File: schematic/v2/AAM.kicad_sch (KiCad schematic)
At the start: 1 part, among them U17 NUCLEO-H753ZI

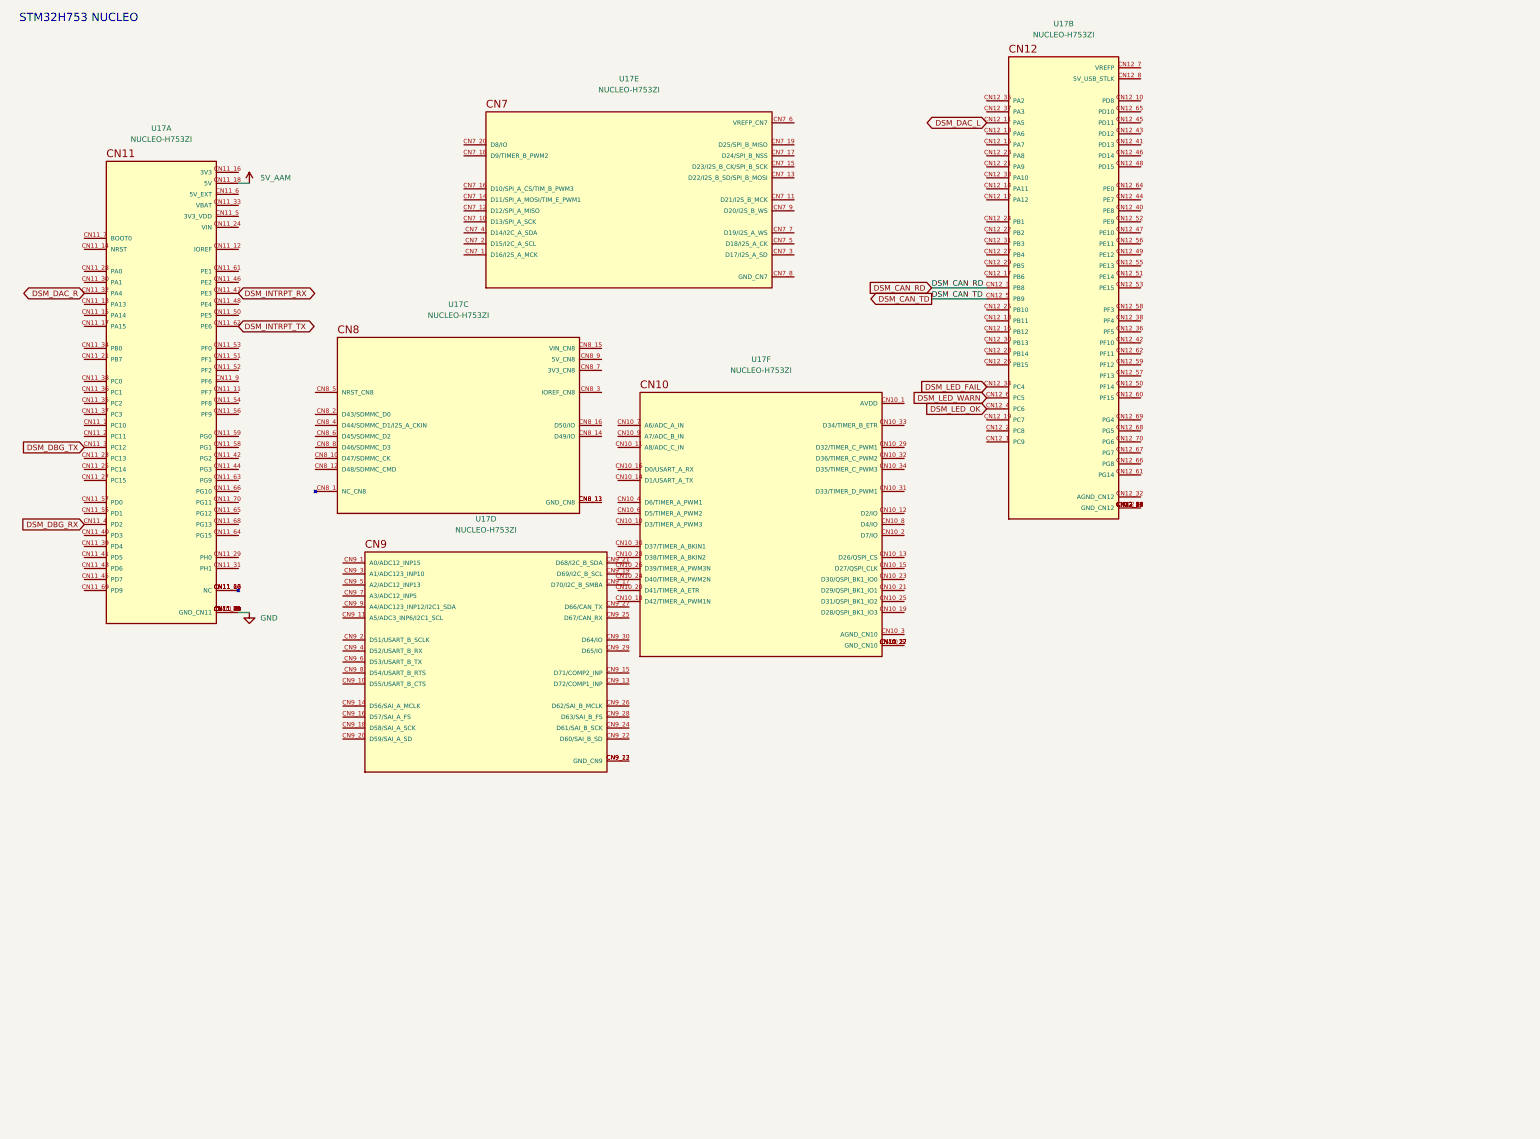
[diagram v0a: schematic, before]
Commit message: moving to multiple sheets for the schematic
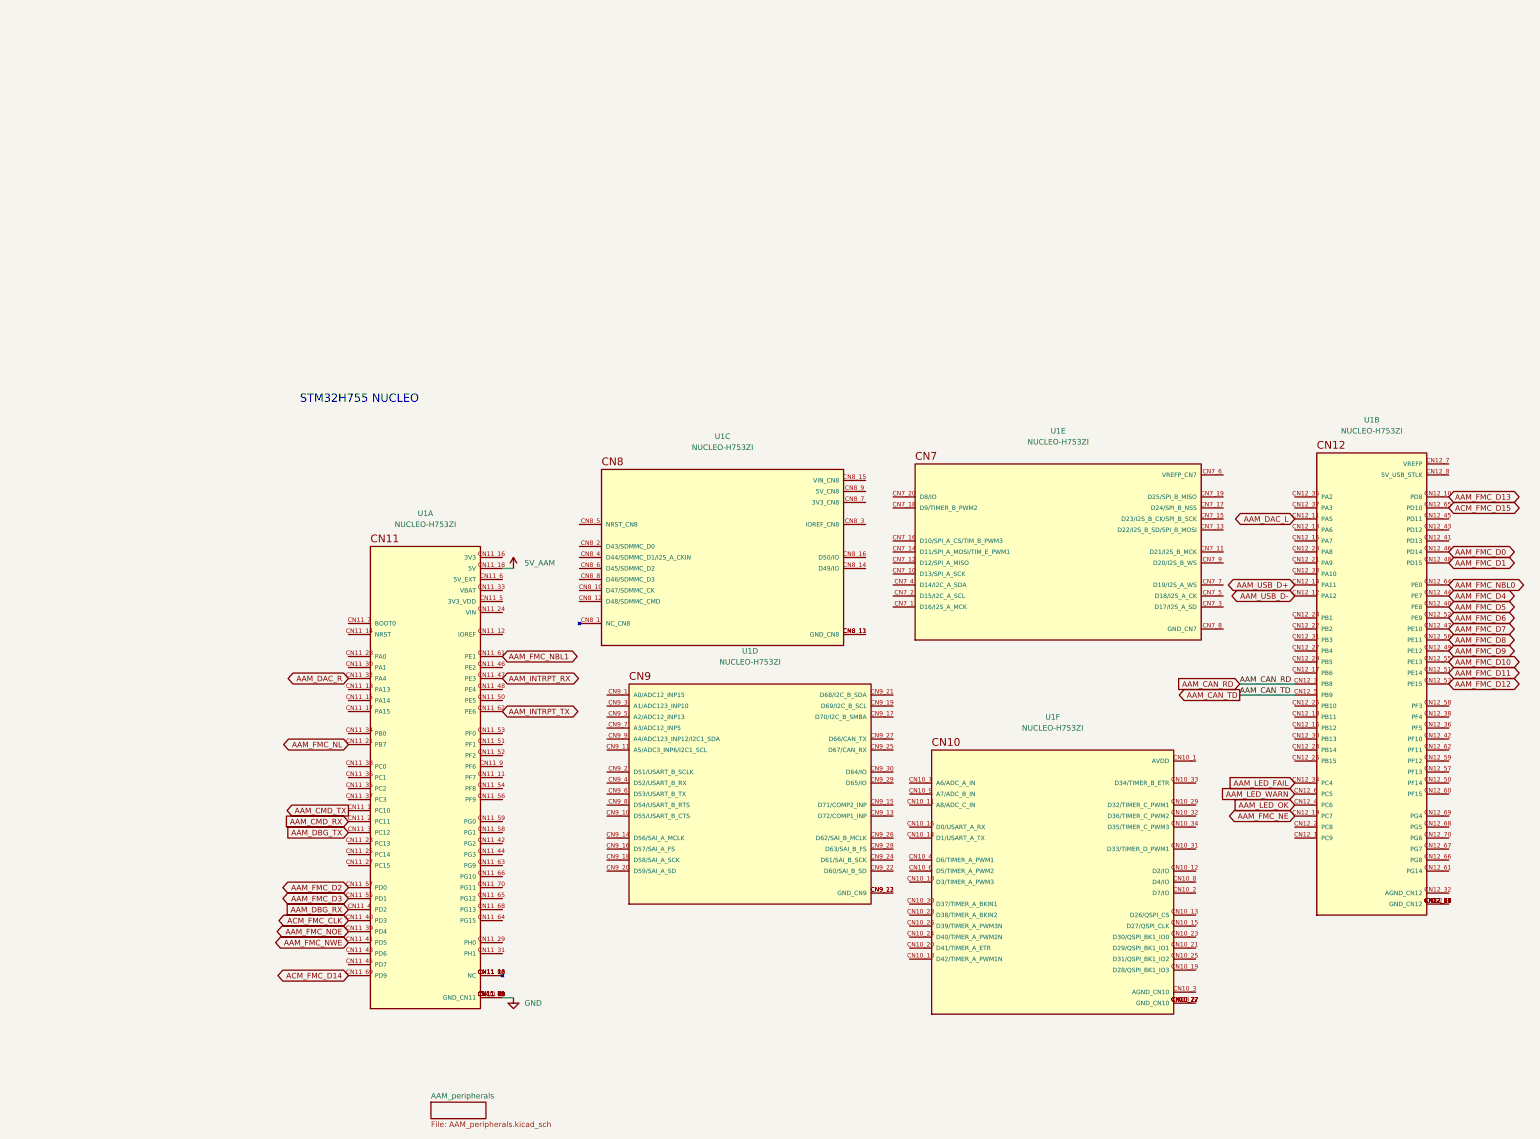
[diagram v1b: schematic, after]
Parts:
- removed U17: NUCLEO-H753ZI, NUCLEO-H753ZI:MODULE_NUCLEO-H753ZI, symbol NUCLEO-H753ZI:NUCLEO-H753ZI
- added U1: NUCLEO-H753ZI, NUCLEO-H753ZI:MODULE_NUCLEO-H753ZI, symbol NUCLEO-H753ZI:NUCLEO-H753ZI
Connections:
- net 5V_AAM: now also U1.CN11_18 (5V)
- net GND: now also U1.CN11_19 (GND_CN11), U1.CN11_20 (GND_CN11), U1.CN11_22 (GND_CN11), U1.CN11_49 (GND_CN11), U1.CN11_60 (GND_CN11), U1.CN11_71 (GND_CN11), U1.CN11_72 (GND_CN11), U1.CN11_8 (GND_CN11)
- new net: U1.CN9_12 (GND_CN9), U1.CN9_23 (GND_CN9)
- new net: U1.CN11_10 (NC), U1.CN11_26 (NC), U1.CN11_67 (NC)
- new net: U1.CN10_17 (GND_CN10), U1.CN10_22 (GND_CN10), U1.CN10_27 (GND_CN10), U1.CN10_5 (GND_CN10)
- new net: U1.CN12_20 (GND_CN12), U1.CN12_39 (GND_CN12), U1.CN12_54 (GND_CN12), U1.CN12_63 (GND_CN12), U1.CN12_71 (GND_CN12), U1.CN12_72 (GND_CN12), U1.CN12_9 (GND_CN12)
- new net: U1.CN8_11 (GND_CN8), U1.CN8_13 (GND_CN8)
- new net AAM_CAN_RD: U1.CN12_3 (PB8)
- new net AAM_CAN_TD: U1.CN12_5 (PB9)
- new net AAM_CMD_RX: U1.CN11_2 (PC11)
- new net AAM_CMD_TX: U1.CN11_1 (PC10)
- new net AAM_DAC_L: U1.CN12_11 (PA5)
- new net AAM_DAC_R: U1.CN11_32 (PA4)
- new net AAM_DBG_RX: U1.CN11_4 (PD2)
- new net AAM_DBG_TX: U1.CN11_3 (PC12)
- new net AAM_FMC_D0: U1.CN12_46 (PD14)
- new net AAM_FMC_D1: U1.CN12_48 (PD15)
- new net AAM_FMC_D10: U1.CN12_55 (PE13)
- new net AAM_FMC_D11: U1.CN12_51 (PE14)
- new net AAM_FMC_D12: U1.CN12_53 (PE15)
- new net AAM_FMC_D13: U1.CN12_10 (PD8)
- new net AAM_FMC_D2: U1.CN11_57 (PD0)
- new net AAM_FMC_D3: U1.CN11_55 (PD1)
- new net AAM_FMC_D4: U1.CN12_44 (PE7)
- new net AAM_FMC_D5: U1.CN12_40 (PE8)
- new net AAM_FMC_D6: U1.CN12_52 (PE9)
- new net AAM_FMC_D7: U1.CN12_47 (PE10)
- new net AAM_FMC_D8: U1.CN12_56 (PE11)
- new net AAM_FMC_D9: U1.CN12_49 (PE12)
- new net AAM_FMC_NBL0: U1.CN12_64 (PE0)
- new net AAM_FMC_NBL1: U1.CN11_61 (PE1)
- new net AAM_FMC_NE: U1.CN12_19 (PC7)
- new net AAM_FMC_NL: U1.CN11_21 (PB7)
- new net AAM_FMC_NOE: U1.CN11_39 (PD4)
- new net AAM_FMC_NWE: U1.CN11_41 (PD5)
- new net AAM_INTRPT_RX: U1.CN11_47 (PE3)
- new net AAM_INTRPT_TX: U1.CN11_62 (PE6)
- new net AAM_LED_FAIL: U1.CN12_34 (PC4)
- new net AAM_LED_OK: U1.CN12_4 (PC6)
- new net AAM_LED_WARN: U1.CN12_6 (PC5)
- new net AAM_USB_D+: U1.CN12_14 (PA11)
- new net AAM_USB_D-: U1.CN12_12 (PA12)
- new net ACM_FMC_CLK: U1.CN11_40 (PD3)
- new net ACM_FMC_D14: U1.CN11_69 (PD9)
- new net ACM_FMC_D15: U1.CN12_65 (PD10)
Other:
- added sheet AAM_peripherals (AAM_peripherals.kicad_sch)
- note added: "STM32H755 NUCLEO"
- note removed: "STM32H753 NUCLEO"

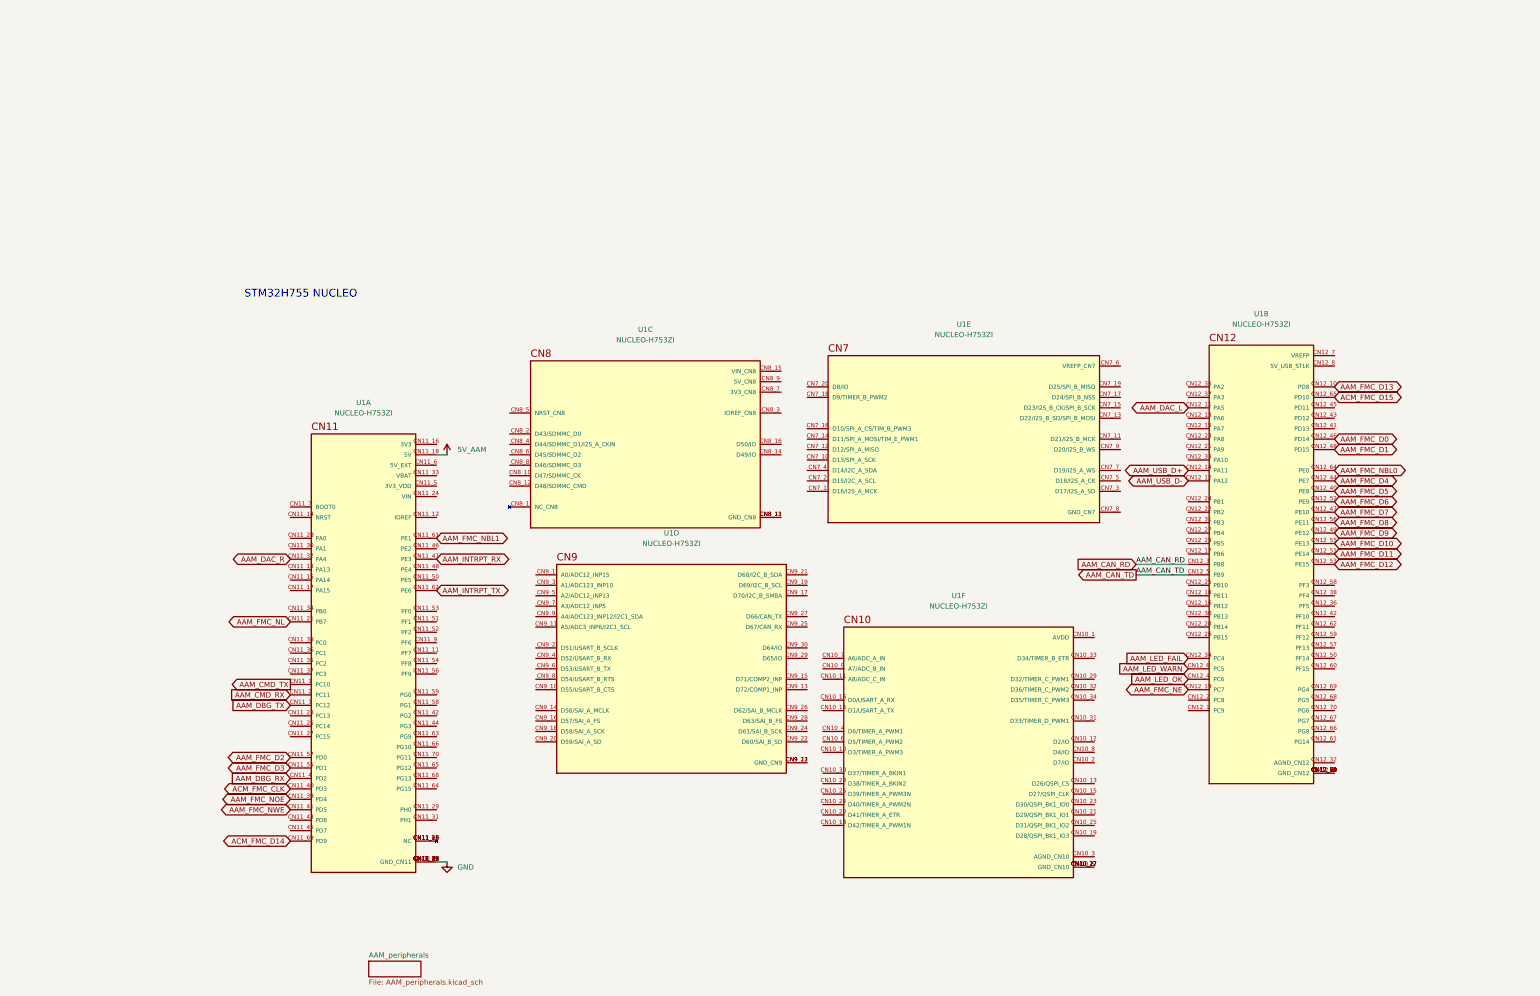
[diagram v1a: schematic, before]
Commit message: adding more sheets in the schematic
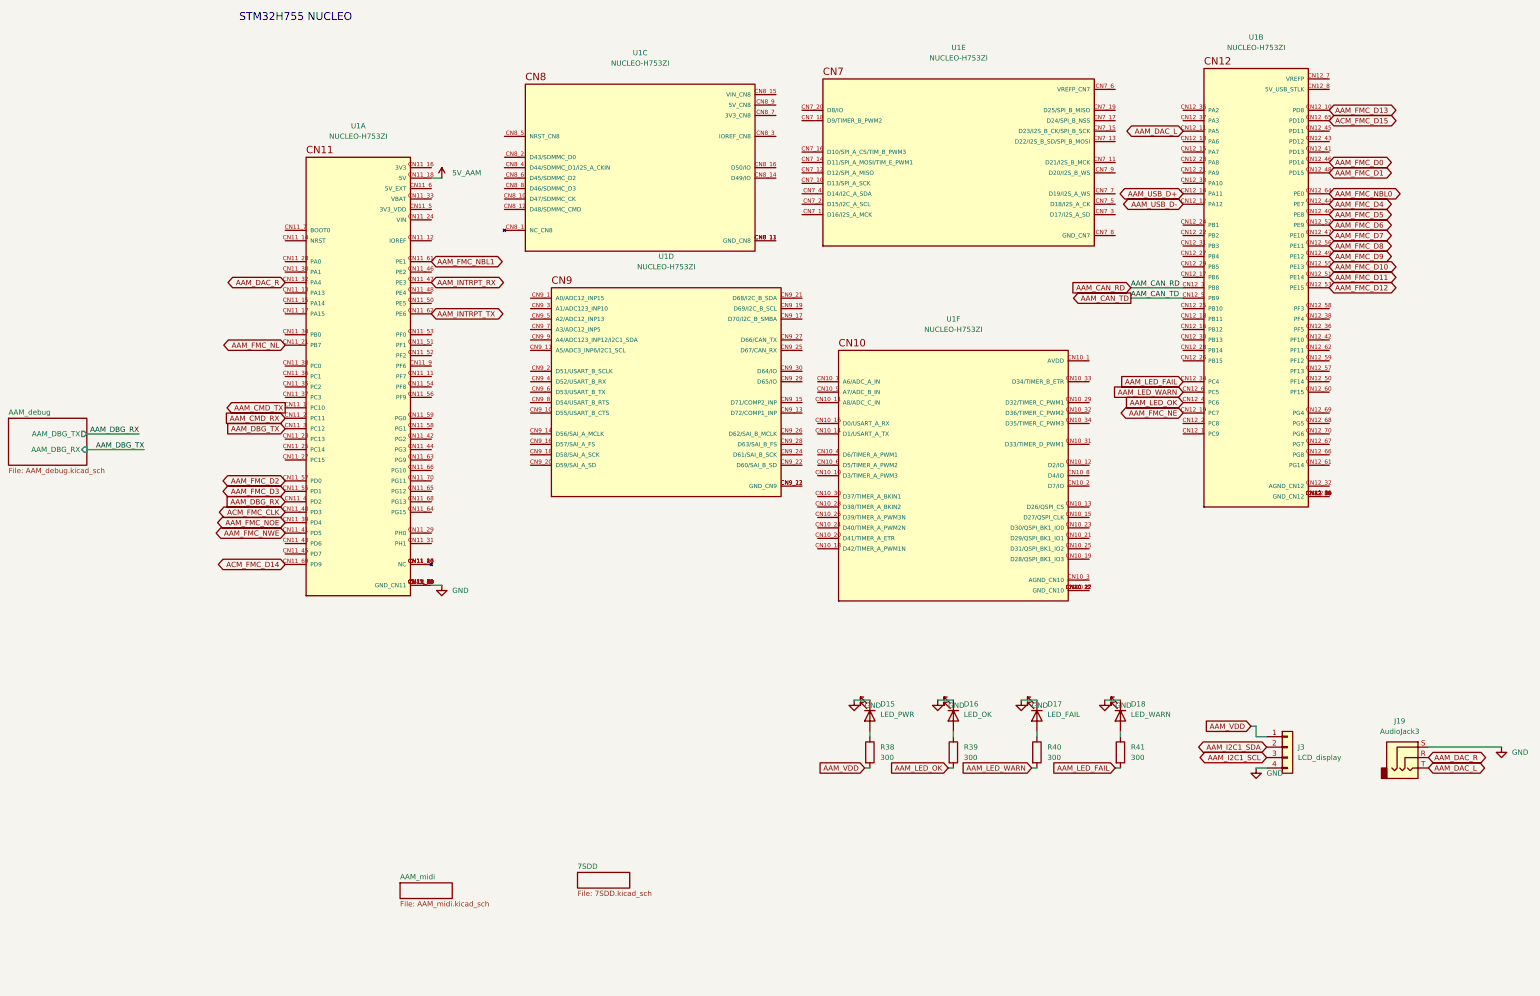
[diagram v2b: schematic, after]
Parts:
- added D15: LED_PWR, LED_SMD:LED_0603_1608Metric, symbol Device:LED
- added D16: LED_OK, LED_SMD:LED_0603_1608Metric, symbol Device:LED
- added D17: LED_FAIL, LED_SMD:LED_0603_1608Metric, symbol Device:LED
- added D18: LED_WARN, LED_SMD:LED_0603_1608Metric, symbol Device:LED
- added J19: AudioJack3, Connector_Audio:Jack_3.5mm_CUI_SJ-3523-SMT_Horizontal, symbol Connector_Audio:AudioJack3
- added J3: LCD_display, Connector_PinHeader_1.00mm:PinHeader_1x04_P1.00mm_Vertical_SMD_Pin1Left, symbol Connector_Generic:Conn_01x04
- added R38, R39, R40, R41: 300, Resistor_SMD:R_0805_2012Metric_Pad1.20x1.40mm_HandSolder, symbol Device:R
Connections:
- net AAM_DAC_L: now also J19.T
- net AAM_DAC_R: now also J19.R
- net AAM_LED_FAIL: now also R41.2
- net AAM_LED_OK: now also R39.2
- net AAM_LED_WARN: now also R40.2
- net GND: now also D15.1 (K), D16.1 (K), D17.1 (K), D18.1 (K), J19.S, J3.4 (Pin_4)
- new net: D18.2 (A), R41.1
- new net: D15.2 (A), R38.1
- new net: D16.2 (A), R39.1
- new net: D17.2 (A), R40.1
- new net AAM_I2C1_SCL: J3.3 (Pin_3)
- new net AAM_I2C1_SDA: J3.2 (Pin_2)
- new net AAM_VDD: J3.1 (Pin_1), R38.2
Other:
- removed sheet AAM_peripherals
- added sheet 7SDD (7SDD.kicad_sch)
- added sheet AAM_debug (AAM_debug.kicad_sch)
- added sheet AAM_midi (AAM_midi.kicad_sch)
- moved on the sheet: U1A, U1B, U1C, U1D, U1E, U1F

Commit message: progress on putting things in different sheets
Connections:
- net ACM_FMC_CLK renamed AAM_FMC_CLK
- net ACM_FMC_D14 renamed AAM_FMC_D14
- net ACM_FMC_D15 renamed AAM_FMC_D15
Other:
- sheet 7SDD ports: added 7SDD_CMD_RX, 7SDD_CMD_TX; removed none
- sheet AAM_midi ports: added AAM_USB_D+, AAM_USB_D-; removed none
- moved on the sheet: D15, D16, D17, D18, J19, J3, R38, R39, R40, R41, U1A, U1B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

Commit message: v2 updates. remove sniffer
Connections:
- net AAM_I2C1_SCL is gone; now on net APM_I2C1_SCL: J3.3 (Pin_3)
- net AAM_I2C1_SDA is gone; now on net APM_I2C1_SDA: J3.2 (Pin_2)
- net APM_I2C1_SCL: now reaches U1.CN11_51 (PF1)
- net APM_I2C1_SDA: now reaches U1.CN11_53 (PF0)
- net 5V_AAM renamed 5V_APM
- net AAM_CAN_RD renamed APM_CAN_RD
- net AAM_CAN_TD renamed APM_CAN_TD
- net AAM_CMD_RX renamed APM_CMD_RX
- net AAM_CMD_TX renamed APM_CMD_TX
- net AAM_DAC_L renamed APM_DAC_L
- net AAM_DAC_R renamed APM_DAC_R
- net AAM_DBG_RX renamed APM_DBG_RX
- net AAM_DBG_TX renamed APM_DBG_TX
- net AAM_FMC_CLK: no longer names the net of U1.CN11_40 (PD3)
- net AAM_FMC_D0: no longer names the net of U1.CN12_46 (PD14)
- net AAM_FMC_D1: no longer names the net of U1.CN12_48 (PD15)
- net AAM_FMC_D10: no longer names the net of U1.CN12_55 (PE13)
- net AAM_FMC_D11: no longer names the net of U1.CN12_51 (PE14)
- net AAM_FMC_D12: no longer names the net of U1.CN12_53 (PE15)
- net AAM_FMC_D13: no longer names the net of U1.CN12_10 (PD8)
- net AAM_FMC_D14: no longer names the net of U1.CN11_69 (PD9)
- net AAM_FMC_D15: no longer names the net of U1.CN12_65 (PD10)
- net AAM_FMC_D2: no longer names the net of U1.CN11_57 (PD0)
- net AAM_FMC_D3: no longer names the net of U1.CN11_55 (PD1)
- net AAM_FMC_D4: no longer names the net of U1.CN12_44 (PE7)
- net AAM_FMC_D5: no longer names the net of U1.CN12_40 (PE8)
- net AAM_FMC_D6: no longer names the net of U1.CN12_52 (PE9)
- net AAM_FMC_D7: no longer names the net of U1.CN12_47 (PE10)
- net AAM_FMC_D8: no longer names the net of U1.CN12_56 (PE11)
- net AAM_FMC_D9: no longer names the net of U1.CN12_49 (PE12)
- net AAM_FMC_NBL0: no longer names the net of U1.CN12_64 (PE0)
- net AAM_FMC_NBL1: no longer names the net of U1.CN11_61 (PE1)
- net AAM_FMC_NE: no longer names the net of U1.CN12_19 (PC7)
- net AAM_FMC_NL: no longer names the net of U1.CN11_21 (PB7)
- net AAM_FMC_NOE: no longer names the net of U1.CN11_39 (PD4)
- net AAM_FMC_NWE: no longer names the net of U1.CN11_41 (PD5)
- net AAM_INTRPT_RX renamed APM_INTRPT_RX
- net AAM_INTRPT_TX renamed APM_INTRPT_TX
- net AAM_LED_FAIL renamed APM_LED_FAIL
- net AAM_LED_OK renamed APM_LED_OK
- net AAM_LED_WARN renamed APM_LED_WARN
- net AAM_USB_D+ renamed APM_USB_D+
- net AAM_USB_D- renamed APM_USB_D-
- net AAM_VDD renamed APM_VDD
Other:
- sheet AAM_debug renamed APM_debug
- sheet AAM_midi renamed APM_midi
- sheet APM_debug: file AAM_debug.kicad_sch -> APM_debug.kicad_sch
- sheet APM_debug ports: added APM_DBG_RX, APM_DBG_TX; removed AAM_DBG_RX, AAM_DBG_TX
- sheet APM_midi: file AAM_midi.kicad_sch -> APM_midi.kicad_sch
- sheet APM_midi ports: added APM_USB_D+, APM_USB_D-; removed AAM_USB_D+, AAM_USB_D-
- moved on the sheet: U1B, U1C, U1D, U1E, U1F
